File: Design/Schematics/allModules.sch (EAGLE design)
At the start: 163 parts, among them IC1 MAX7219CNG, IC2 MAX7219CNG, IC3 MAX7219CNG, IC4 MAX7219CNG, SW1 arcade_btn, SW2 arcade_btn, SW3 arcade_btn, SW4 arcade_btn, U1 328P, U2 328P, U3 328P, U4 328P, U5 328P, U6 328P

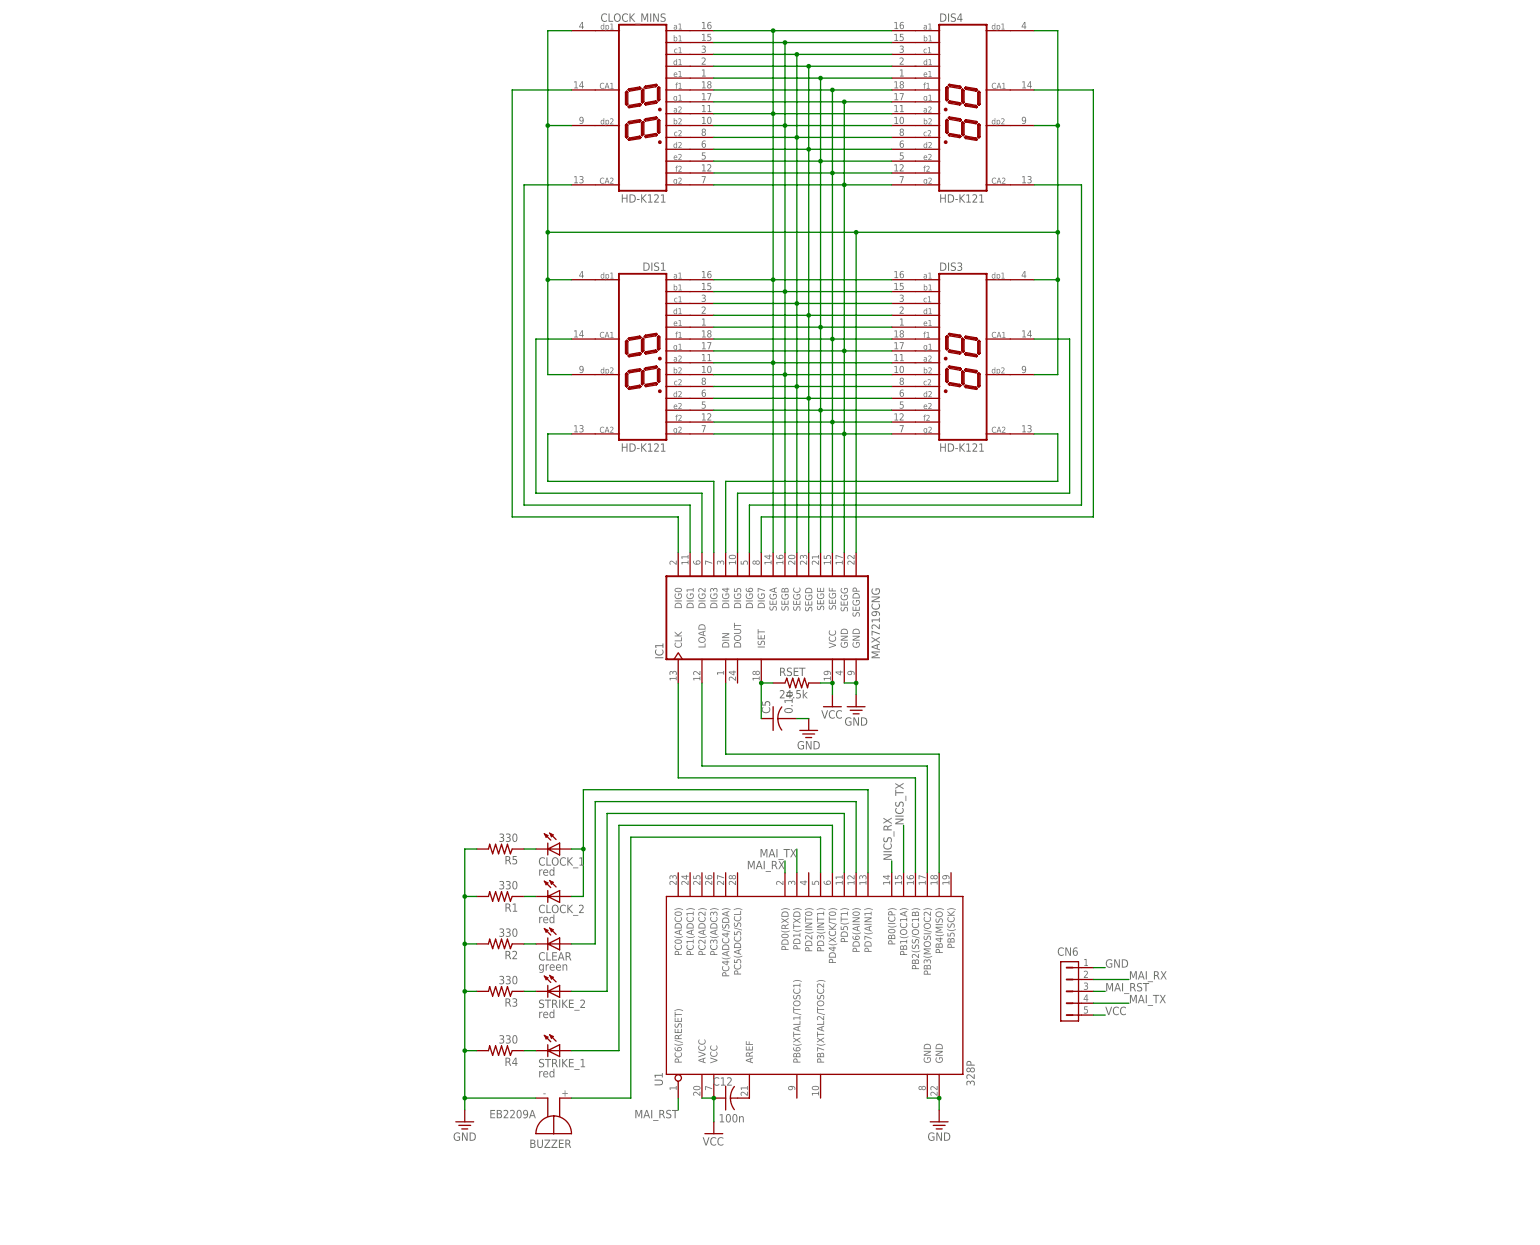
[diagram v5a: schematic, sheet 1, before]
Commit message: Added frames to all modules
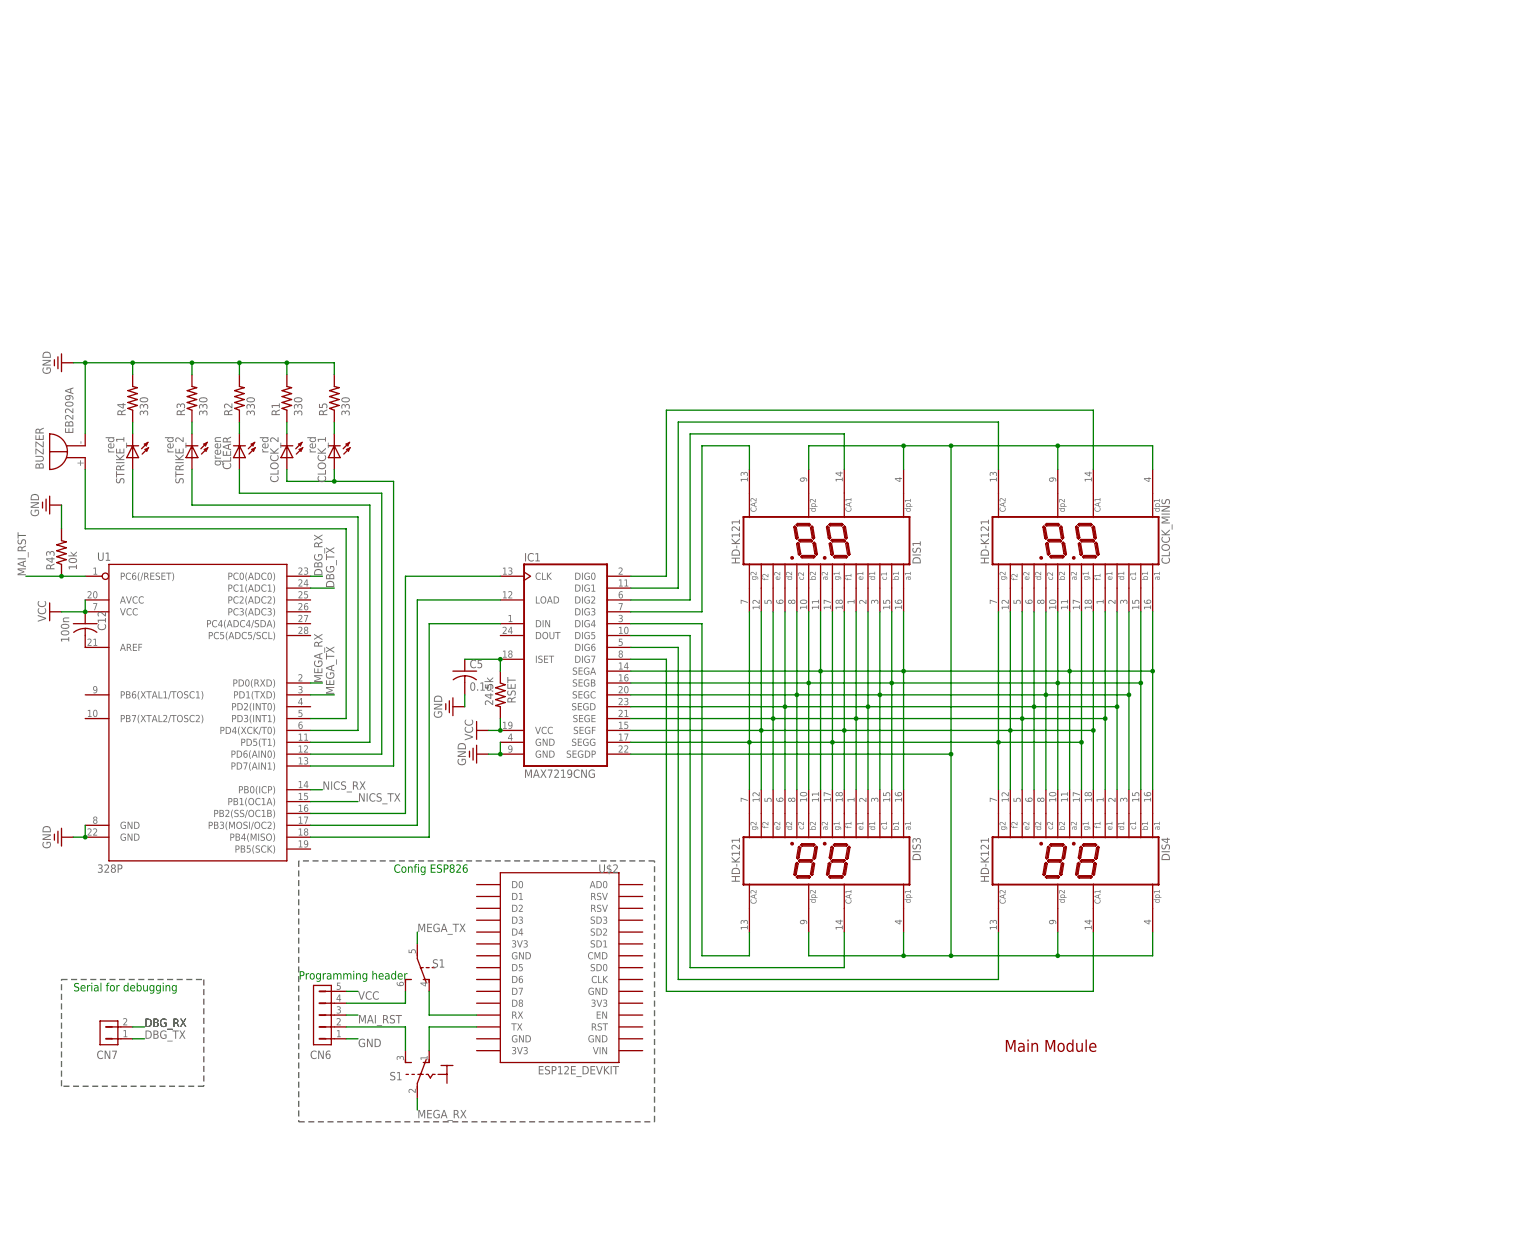
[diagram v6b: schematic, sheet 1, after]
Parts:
- added CN7: (no value), con-hdrs40:HDR-1X2-MTA-100
- added R43, R44, R45, R46, R47, R48: 10k, adafruit:R-US_0309/12
- added S1: (no value), switch:320-938
- added U$2: ESP12E_DEVKIT, ESP12E_DEVKIT:ESP12E_DEVKIT
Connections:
- removed net MAI_RX: CN6.2, U1.PD0(RXD)
- removed net MAI_TX: CN6.4, U1.PD1(TXD)
- new net DBG_RX: CN7.2, U1.PC0(ADC0)
- new net DBG_TX: CN7.1, U1.PC1(ADC1)
- new net MEGA_RX: S11.P, U1.PD0(RXD)
- new net MEGA_TX: S1B.P, U1.PD1(TXD)
- new net N$141: CN6.4, S1B.S
- new net N$142: CN6.2, S11.S
- new net N$32: S11.O, U$2.TX
- new net N$33: S1B.O, U$2.RX
- net BTN_RST: now also R47.1
- net GND: now also R43.2, R44.2, R45.2, R46.2, R47.2, R48.2
- net MAI_RST: now also R43.1
- net MEM_RST: now also R48.1
- net MZE_RST: now also R45.1
- net SAY_RST: now also R44.1
- net SW_RST: now also R46.1
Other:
- note added: "Button Module"
- note added: "Config ESP826"
- note added: "Main Module"
- note added: "Maze Module"
- note added: "Memory Module"
- note added: "Programming header"
- note added: "Serial for debugging"
- note added: "Simon Says Module"
- note added: "Simple Wires Module"
- moved on the sheet: BIG_BTN, BIG_BTN_CHAR, BIG_NUM, BLUE, BUTTON_LED, BUZZER, C1, C10, C11, C12, C2, C3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

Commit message: Updated schematic
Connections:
- net GND: no longer R43.2, R44.2, R45.2, R46.2, R47.2, R48.2
- net VCC: now also R43.2, R44.2, R45.2, R46.2, R47.2, R48.2

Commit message: Updated schematic to add serial displays
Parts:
- removed DIS3, DIS4: HD-K121, display-hp:HD-K121
- added C13: 100n, adafruit:C-US025-024X044
- added C14: 47u, adafruit:C-US025-024X044
- added CSET: 22p, adafruit:C-US025-024X044
- added MAX6954: MAX6954, MAX6954:MAX6954
- added RSET2: 56k, BeagleBone_Black_Wireless:R-US_0204/7
- added SERIAL_1, SERIAL_2, SERIAL_3: XAMR14C2, MAX6954:XAMR14C2
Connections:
- removed net N$10 (its old number): DIS4.CA2, IC1.DIG6
- removed net N$17: IC1.CLK, U1.PB2(SS/OC1B)
- removed net N$18: IC1.DIN, U1.PB4(MISO)
- new net O0: MAX6954.O0, SERIAL_1.CC1, SERIAL_2.A, SERIAL_3.A
- new net O1: MAX6954.O1, SERIAL_1.CC2
- new net O10: MAX6954.O10, SERIAL_1.G, SERIAL_2.G, SERIAL_3.G
- new net O11: MAX6954.O11, SERIAL_1.H, SERIAL_2.H, SERIAL_3.H
- new net O12: MAX6954.O12, SERIAL_1.J, SERIAL_2.J, SERIAL_3.J
- new net O13: MAX6954.O13, SERIAL_1.K, SERIAL_2.K, SERIAL_3.K
- new net O14: MAX6954.O14, SERIAL_1.L, SERIAL_2.L, SERIAL_3.L
- new net O15: MAX6954.O15, SERIAL_1.M, SERIAL_2.M, SERIAL_3.M
- new net O16: MAX6954.O16, SERIAL_1.N, SERIAL_2.N, SERIAL_3.N
- new net O17: MAX6954.O17, SERIAL_1.P, SERIAL_2.P, SERIAL_3.P
- new net O2: MAX6954.O2, SERIAL_1.A, SERIAL_2.CC1, SERIAL_3.B
- new net O3: MAX6954.O3, SERIAL_2.CC2, SERIAL_3.C
- new net O4: MAX6954.O4, SERIAL_1.B, SERIAL_2.B, SERIAL_3.CC1
- new net O5: MAX6954.O5, SERIAL_1.C, SERIAL_2.C, SERIAL_3.CC2
- new net O6: MAX6954.O6, SERIAL_1.D, SERIAL_2.D, SERIAL_3.D
- new net O7: MAX6954.O7
- new net O8: MAX6954.O8, SERIAL_1.E, SERIAL_2.E, SERIAL_3.E
- new net O9: MAX6954.O9, SERIAL_1.F, SERIAL_2.F, SERIAL_3.F
- new net SERIAL_CLK: MAX6954.CLK, U1.PC4(ADC4/SDA)
- new net SERIAL_CS: MAX6954.CS, U1.PC2(ADC2)
- new net SERIAL_DIN: MAX6954.DIN, U1.PC3(ADC3)
- net GND: now also C13.2, C14.2, CSET.2, MAX6954.GND@1, MAX6954.GND@2, MAX6954.GND@3, RSET2.1
- net N$1: no longer DIS3.A1, DIS3.A2, DIS4.A1, DIS4.A2
- net N$11: now also IC1.DIN, U1.PB2(SS/OC1B); no longer DIS3.CA1, IC1.DIG5
- net N$12: now also IC1.CLK, U1.PB4(MISO); no longer DIS3.CA2, IC1.DIG4
- net N$2: no longer DIS3.B1, DIS3.B2, DIS4.B1, DIS4.B2
- net N$3: no longer DIS3.C1, DIS3.C2, DIS4.C1, DIS4.C2
- net N$4: no longer DIS3.D1, DIS3.D2, DIS4.D1, DIS4.D2
- net N$5: no longer DIS3.E1, DIS3.E2, DIS4.E1, DIS4.E2
- net N$6: no longer DIS3.F1, DIS3.F2, DIS4.F1, DIS4.F2
- net N$7: no longer DIS3.G1, DIS3.G2, DIS4.G1, DIS4.G2
- net N$8: now also CSET.1, MAX6954.OSC; no longer CLOCK_MINS.DP1, CLOCK_MINS.DP2, DIS1.DP1, DIS1.DP2, DIS3.DP1, DIS3.DP2, DIS4.DP1, DIS4.DP2, IC1.SEGDP
- net N$9: now also MAX6954.ISET, RSET2.2; no longer DIS4.CA1, IC1.DIG7
- net VCC: now also C13.1, C14.1, MAX6954.V+@1, MAX6954.V+@2, MAX6954.V+@3
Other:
- note added: "Config Module"
- note removed: "Config ESP826"
